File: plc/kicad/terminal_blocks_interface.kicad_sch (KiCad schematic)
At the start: 79 parts, among them CN1 DB128V-5.08-2P-GN-S, CN10 DB128V-5.08-6P-GN-S, CN2 DB128V-5.08-2P-GN-S, CN3 DB128V-5.08-2P-GN-S, CN4 DB128V-5.08-2P-GN-S, CN5 DB128V-5.08-2P-GN-S, CN6 DB128V-5.08-2P-GN-S, CN7 DB128V-5.08-2P-GN-S, CN8 DB128V-5.08-2P-GN-S, CN9 DB128V-5.08-2P-GN-S, Q1 AO3400A, Q2 AO3400A, U1 TCA9535PWR, U2 TPS272C45DRHFR, U3 TPS272C45DRHFR, U4 ADS1115IDGSR, U5 LTV-814S-TA1-A, U6 LTV-814S-TA1-A, U7 LTV-814S-TA1-A, U8 LTV-814S-TA1-A

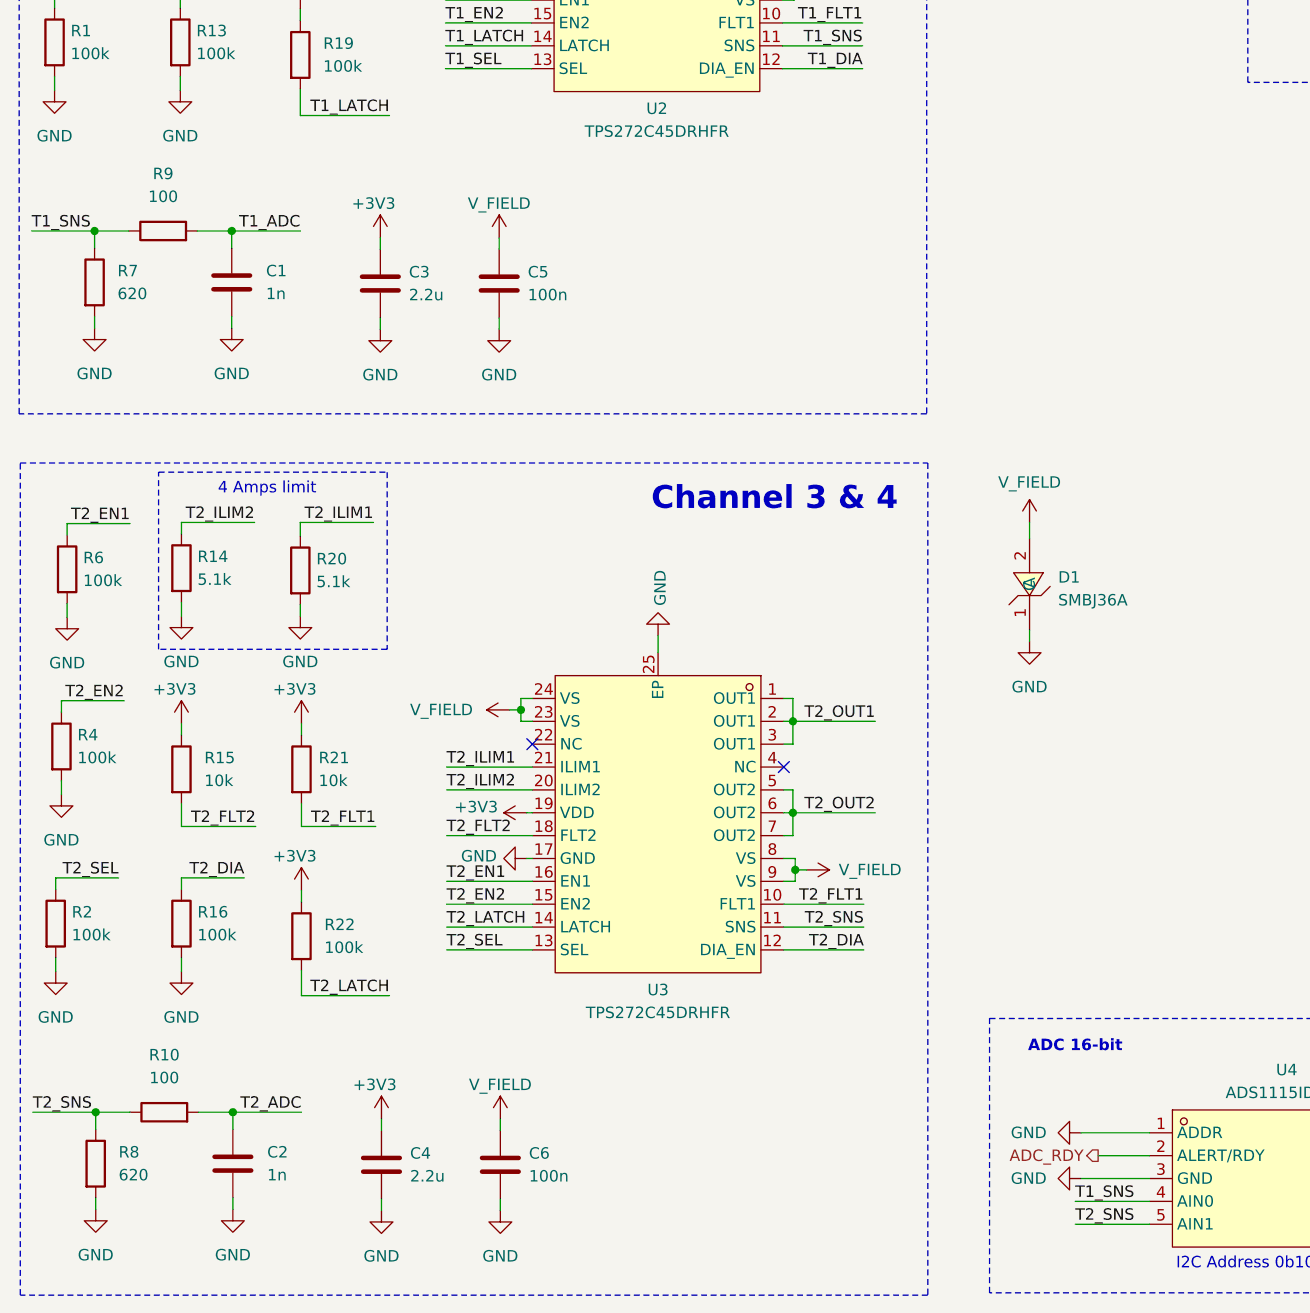
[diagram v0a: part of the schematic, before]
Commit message: Fixed ADC pins & rc filter
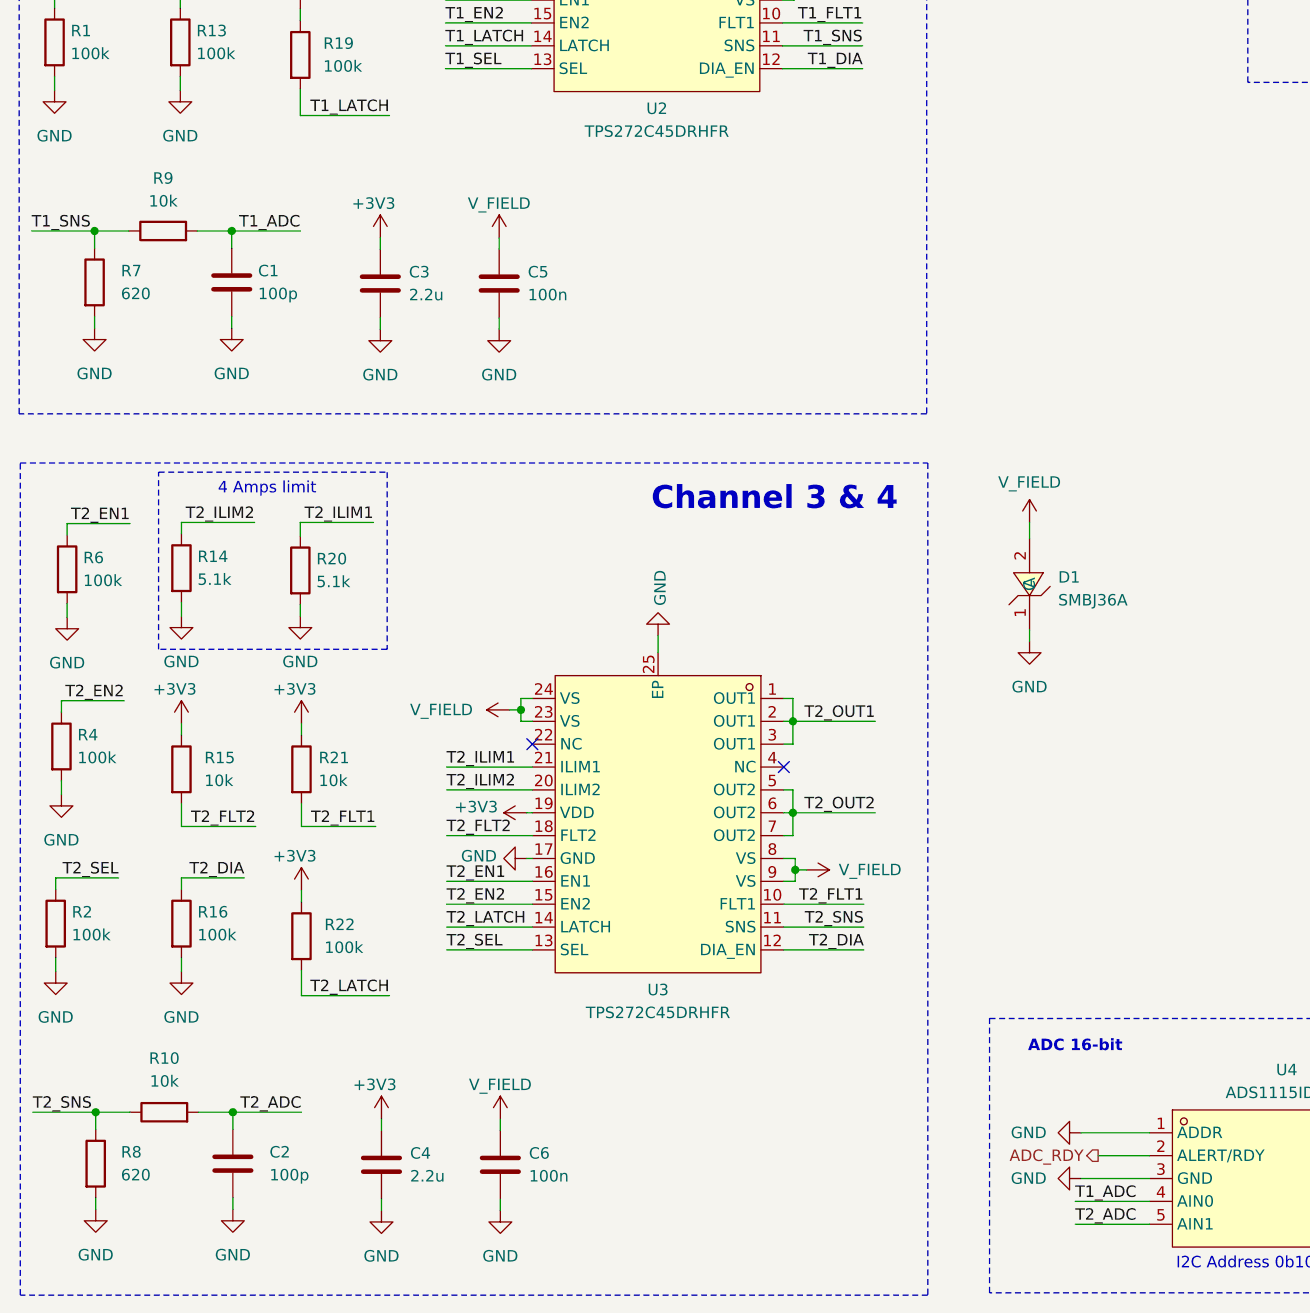
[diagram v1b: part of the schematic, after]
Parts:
- C1, C2: value 1n -> 100p
- R10, R9: value 100 -> 10k
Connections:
- net T1_ADC: now also U4.4 (AIN0)
- net T1_SNS: no longer U4.4 (AIN0)
- net T2_ADC: now also U4.5 (AIN1)
- net T2_SNS: no longer U4.5 (AIN1)
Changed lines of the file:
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@@
 		)
 	)
-	(label "T1_SNS"
+	(label "T1_ADC"
 		(at 136.525 267.335 0)
 		(effects
@@
 		)
 	)
-	(label "T2_SNS"
+	(label "T2_ADC"
 		(at 136.525 269.875 0)
 		(effects
@@
 		(fields_autoplaced yes)
 		(property "Reference" "C1"
-			(at 46.609 163.9569 0)
+			(at 45.72 163.9569 0)
 			(show_name no)
 			(do_not_autoplace no)
@@
 			)
 		)
-		(property "Value" "1n"
-			(at 46.609 166.4969 0)
+		(property "Value" "100p"
+			(at 45.72 166.4969 0)
 			(show_name no)
 			(do_not_autoplace no)
@@
 		(fields_autoplaced yes)
 		(property "Reference" "R8"
-			(at 30.226 261.8739 0)
+			(at 30.48 261.8739 0)
 			(show_name no)
 			(do_not_autoplace no)
@@
 		)
 		(property "Value" "620"
-			(at 30.226 264.4139 0)
+			(at 30.48 264.4139 0)
 			(show_name no)
 			(do_not_autoplace no)
@@
 		(fields_autoplaced yes)
 		(property "Reference" "R9"
-			(at 35.179 153.162 90)
+			(at 35.179 153.67 90)
 			(show_name no)
 			(do_not_autoplace no)
@@
 			)
 		)
-		(property "Value" "100"
-			(at 35.179 155.702 90)
+		(property "Value" "10k"
+			(at 35.179 156.21 90)
 			(show_name no)
 			(do_not_autoplace no)
@@
 		(fields_autoplaced yes)
 		(property "Reference" "R10"
-			(at 35.306 251.079 90)
+			(at 35.306 251.46 90)
 			(show_name no)
 			(do_not_autoplace no)
@@
 			)
 		)
-		(property "Value" "100"
-			(at 35.306 253.619 90)
+		(property "Value" "10k"
+			(at 35.306 254 90)
 			(show_name no)
 			(do_not_autoplace no)
@@
 		(fields_autoplaced yes)
 		(property "Reference" "C2"
-			(at 46.736 261.8739 0)
+			(at 46.99 261.8739 0)
 			(show_name no)
 			(do_not_autoplace no)
@@
 			)
 		)
-		(property "Value" "1n"
-			(at 46.736 264.4139 0)
+		(property "Value" "100p"
+			(at 46.99 264.4139 0)
 			(show_name no)
 			(do_not_autoplace no)
@@
 		(fields_autoplaced yes)
 		(property "Reference" "R7"
-			(at 30.099 163.9569 0)
+			(at 30.48 163.9569 0)
 			(show_name no)
 			(do_not_autoplace no)
@@
 		)
 		(property "Value" "620"
-			(at 30.099 166.4969 0)
+			(at 30.48 166.4969 0)
 			(show_name no)
 			(do_not_autoplace no)

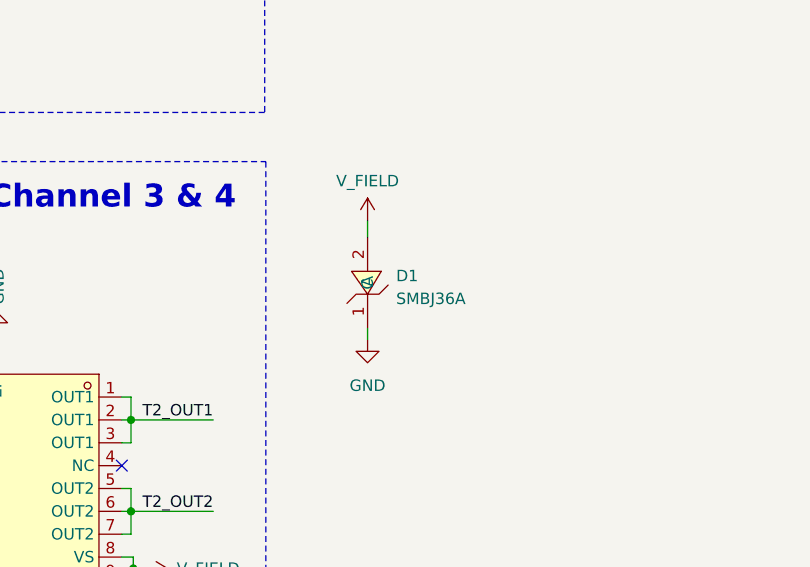
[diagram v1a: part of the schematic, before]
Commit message: Eliminated series diode to output transistors
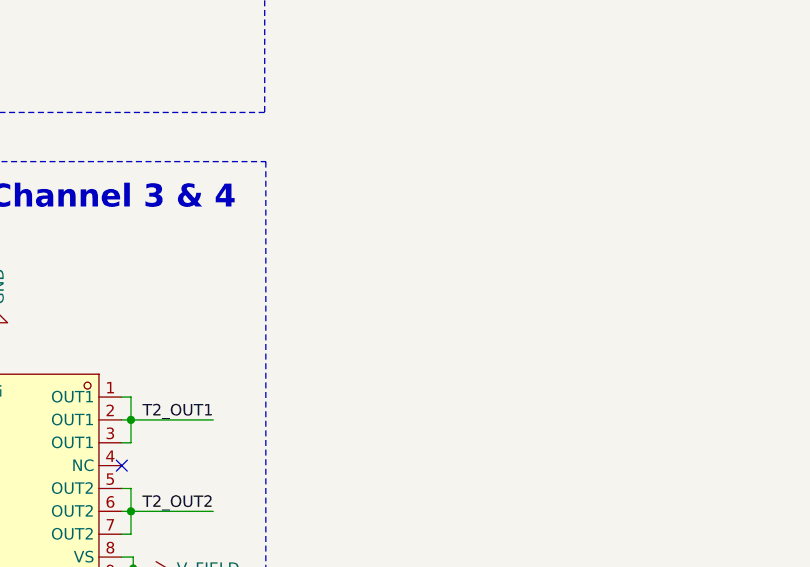
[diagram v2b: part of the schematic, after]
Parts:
- removed D1: SMBJ36A, LibrePLC32:SMB_L4.6-W3.6-LS5.3-RD, symbol LibrePLC32:SMBJ36A-C114001

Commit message: TPS7A52-Q1 PCB placement
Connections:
- net +5V renamed ++5V
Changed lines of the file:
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@@
 			)
 		)
-		(property "Value" "+5V"
+		(property "Value" "++5V"
 			(at 335.915 50.165 0)
 			(show_name no)
@@
 			)
 		)
-		(property "Value" "+5V"
+		(property "Value" "++5V"
 			(at 335.915 22.225 0)
 			(show_name no)
